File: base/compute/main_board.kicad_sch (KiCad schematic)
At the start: 19 parts, among them J1 USB_C_Receptacle_USB2.0_16P, J3 Conn_02x20_Counter_Clockwise, U1 MCP1700T-1202ETT, U3 LD1117S33TR_SOT223

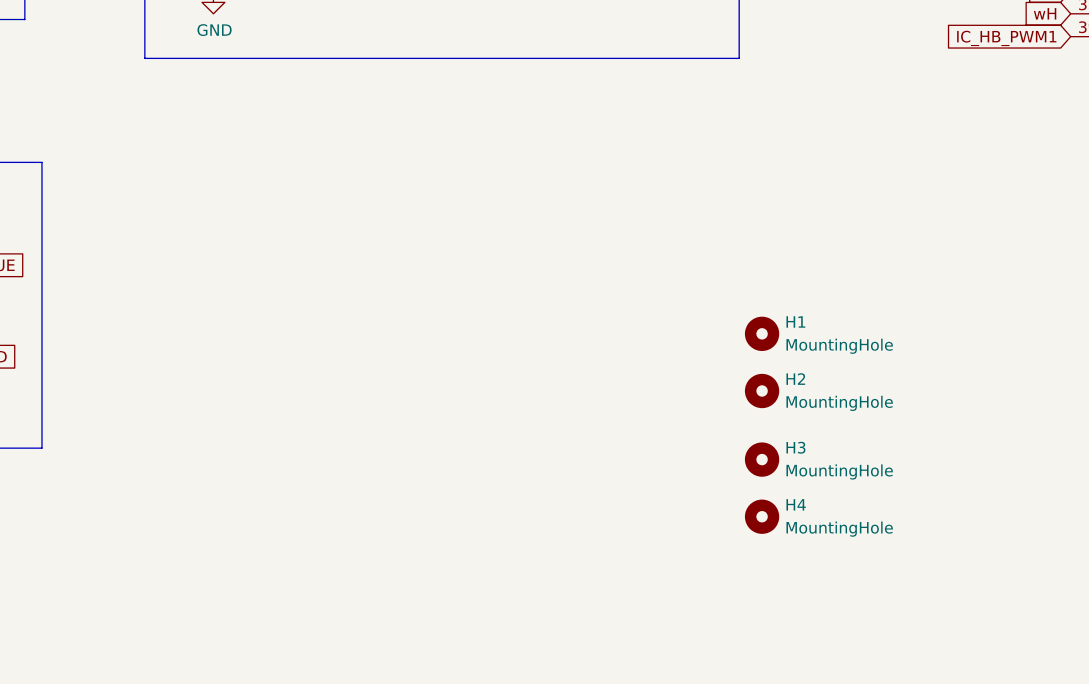
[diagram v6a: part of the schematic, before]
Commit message: added mount felixprinter, standoffs
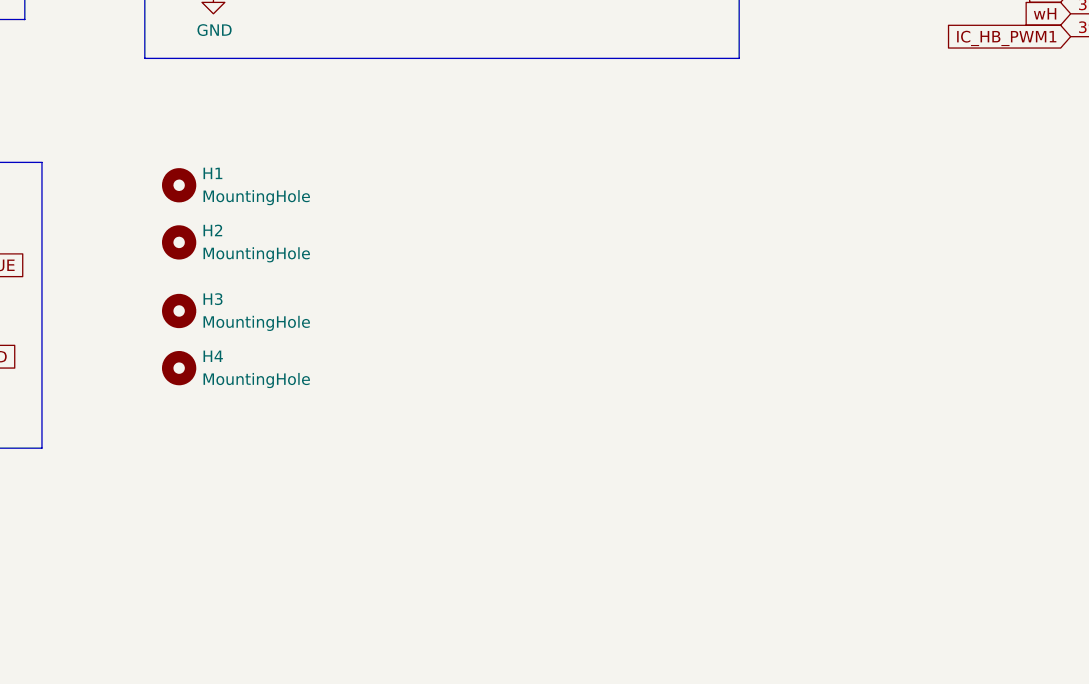
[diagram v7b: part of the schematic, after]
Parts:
- H1, H2, H3, H4: manf# (none) -> 970050244; mouser# (none) -> 710-970050244
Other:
- moved on the sheet: H1, H2, H3, H4
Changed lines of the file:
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@@
 	(symbol
 		(lib_id "Mechanical:MountingHole")
-		(at 182.88 121.92 0)
+		(at 118.11 105.41 0)
 		(unit 1)
 		(exclude_from_sim yes)
@@
 		(fields_autoplaced yes)
 		(property "Reference" "H2"
-			(at 185.42 120.6499 0)
+			(at 120.65 104.1399 0)
 			(effects
 				(font
@@
 		)
 		(property "Value" "MountingHole"
-			(at 185.42 123.1899 0)
+			(at 120.65 106.6799 0)
 			(effects
 				(font
@@
 		)
 		(property "Footprint" "MountingHole:MountingHole_2.2mm_M2"
-			(at 182.88 121.92 0)
+			(at 118.11 105.41 0)
 			(effects
 				(font
@@
 		)
 		(property "Datasheet" "~"
-			(at 182.88 121.92 0)
+			(at 118.11 105.41 0)
 			(effects
 				(font
@@
 		)
 		(property "Description" "Mounting Hole without connection"
-			(at 182.88 121.92 0)
+			(at 118.11 105.41 0)
+			(effects
+				(font
+					(size 1.27 1.27)
+				)
+				(hide yes)
+			)
+		)
+		(property "manf#" "970050244"
+			(at 118.11 105.41 0)
+			(effects
+				(font
+					(size 1.27 1.27)
+				)
+				(hide yes)
+			)
+		)
+		(property "mouser#" "710-970050244"
+			(at 118.11 105.41 0)
 			(effects
 				(font
@@
 	(symbol
 		(lib_id "Mechanical:MountingHole")
-		(at 182.88 129.54 0)
+		(at 118.11 113.03 0)
 		(unit 1)
 		(exclude_from_sim yes)
@@
 		(fields_autoplaced yes)
 		(property "Reference" "H3"
-			(at 185.42 128.2699 0)
+			(at 120.65 111.7599 0)
 			(effects
 				(font
@@
 		)
 		(property "Value" "MountingHole"
-			(at 185.42 130.8099 0)
+			(at 120.65 114.2999 0)
 			(effects
 				(font
@@
 		)
 		(property "Footprint" "MountingHole:MountingHole_2.2mm_M2"
-			(at 182.88 129.54 0)
+			(at 118.11 113.03 0)
 			(effects
 				(font
@@
 		)
 		(property "Datasheet" "~"
-			(at 182.88 129.54 0)
+			(at 118.11 113.03 0)
 			(effects
 				(font
@@
 		)
 		(property "Description" "Mounting Hole without connection"
-			(at 182.88 129.54 0)
+			(at 118.11 113.03 0)
+			(effects
+				(font
+					(size 1.27 1.27)
+				)
+				(hide yes)
+			)
+		)
+		(property "manf#" "970050244"
+			(at 118.11 113.03 0)
+			(effects
+				(font
+					(size 1.27 1.27)
+				)
+				(hide yes)
+			)
+		)
+		(property "mouser#" "710-970050244"
+			(at 118.11 113.03 0)
 			(effects
 				(font
@@
 	(symbol
 		(lib_id "Mechanical:MountingHole")
-		(at 182.88 115.57 0)
+		(at 118.11 99.06 0)
 		(unit 1)
 		(exclude_from_sim yes)
@@
 		(fields_autoplaced yes)
 		(property "Reference" "H1"
-			(at 185.42 114.2999 0)
+			(at 120.65 97.7899 0)
 			(effects
 				(font
@@
 		)
 		(property "Value" "MountingHole"
-			(at 185.42 116.8399 0)
+			(at 120.65 100.3299 0)
 			(effects
 				(font
@@
 		)
 		(property "Footprint" "MountingHole:MountingHole_2.2mm_M2"
-			(at 182.88 115.57 0)
+			(at 118.11 99.06 0)
 			(effects
 				(font
@@
 		)
 		(property "Datasheet" "~"
-			(at 182.88 115.57 0)
+			(at 118.11 99.06 0)
 			(effects
 				(font
@@
 		)
 		(property "Description" "Mounting Hole without connection"
-			(at 182.88 115.57 0)
+			(at 118.11 99.06 0)
+			(effects
+				(font
+					(size 1.27 1.27)
+				)
+				(hide yes)
+			)
+		)
+		(property "mouser#" "710-970050244"
+			(at 118.11 99.06 0)
+			(effects
+				(font
+					(size 1.27 1.27)
+				)
+				(hide yes)
+			)
+		)
+		(property "manf#" "970050244"
+			(at 118.11 99.06 0)
 			(effects
 				(font
@@
 	(symbol
 		(lib_id "Mechanical:MountingHole")
-		(at 182.88 135.89 0)
+		(at 118.11 119.38 0)
 		(unit 1)
 		(exclude_from_sim yes)
@@
 		(fields_autoplaced yes)
 		(property "Reference" "H4"
-			(at 185.42 134.6199 0)
+			(at 120.65 118.1099 0)
 			(effects
 				(font
@@
 		)
 		(property "Value" "MountingHole"
-			(at 185.42 137.1599 0)
+			(at 120.65 120.6499 0)
 			(effects
 				(font
@@
 		)
 		(property "Footprint" "MountingHole:MountingHole_2.2mm_M2"
-			(at 182.88 135.89 0)
+			(at 118.11 119.38 0)
 			(effects
 				(font
@@
 		)
 		(property "Datasheet" "~"
-			(at 182.88 135.89 0)
+			(at 118.11 119.38 0)
 			(effects
 				(font
@@
 		)
 		(property "Description" "Mounting Hole without connection"
-			(at 182.88 135.89 0)
-			(effects
-				(font
+			(at 118.11 119.38 0)
+			(effects
+				(font
+					(size 1.27 1.27)
+				)
+				(hide yes)
+			)
+		)
+		(property "manf#" "970050244"
+			(at 118.11 119.38 0)
+			(effects
+				(font
+					(size 1.27 1.27)
+				)
+				(hide yes)
+			)
+		)
+		(property "mouser#" "710-970050244"
+			(at 118.11 119.38 0)
+			(effects
+				(font
